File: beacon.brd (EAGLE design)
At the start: 40 x 25.3 mm, 49 parts, among them J1 5-5530843-0MALE, Q1 MMBT3904, Q2 DMG2302UK, U1 AOZ6662DI, U3 ATTINY85, U4 MS5637-02BA03, U5 SI4012, U6 MAAL-010704, U7 MIC5504

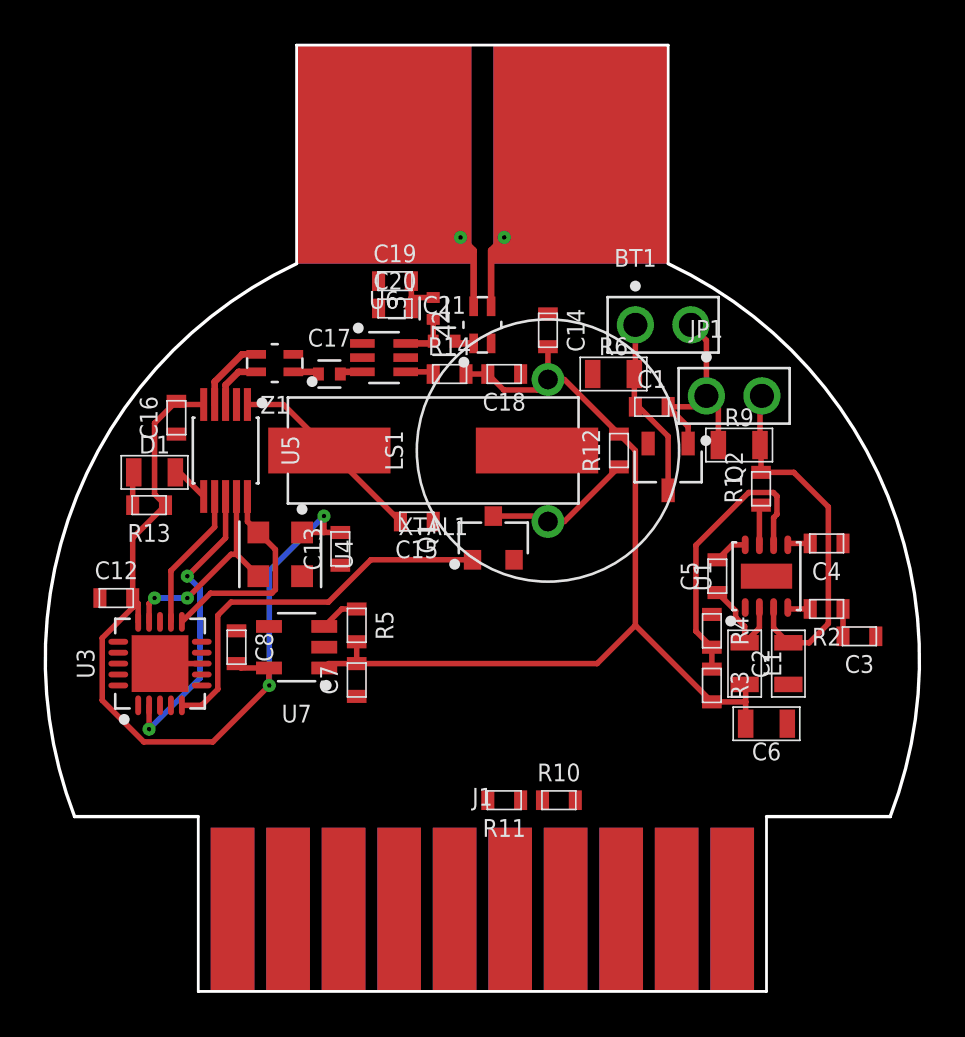
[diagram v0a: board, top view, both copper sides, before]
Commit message: Routed beacon
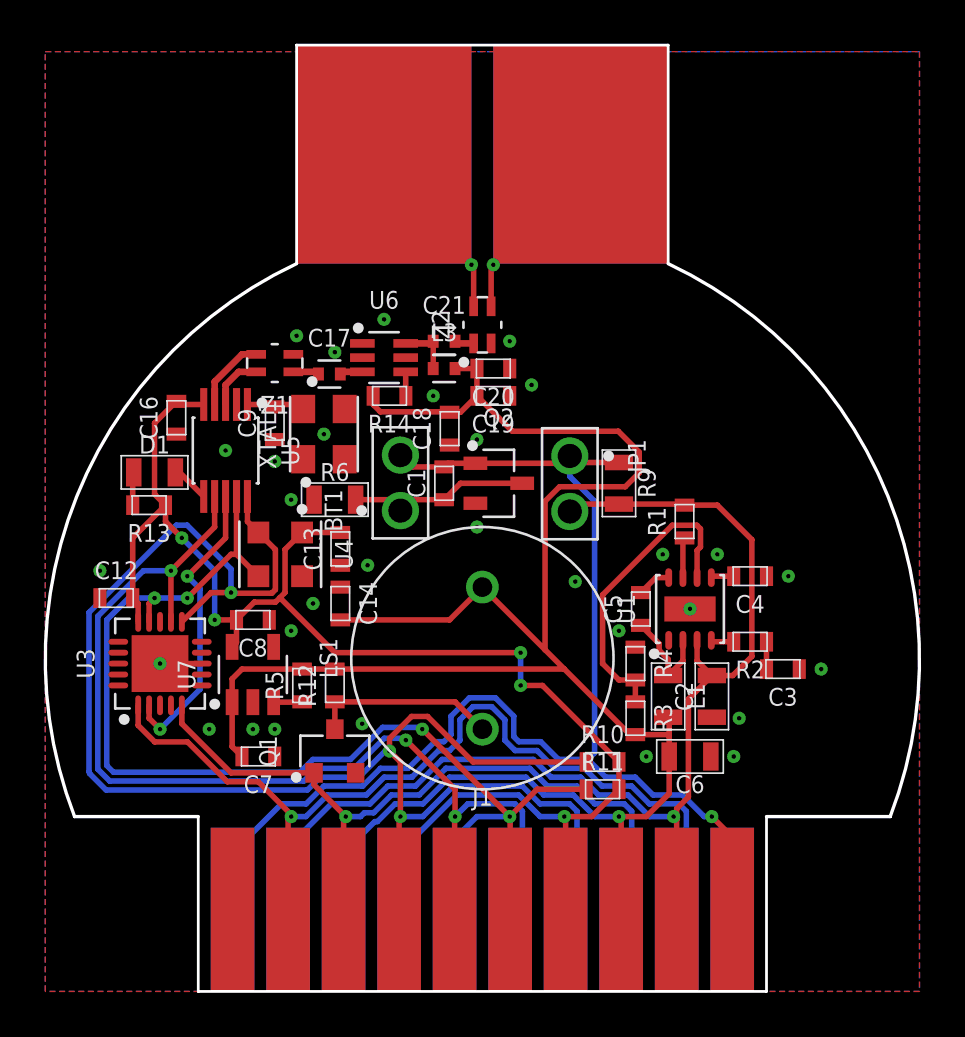
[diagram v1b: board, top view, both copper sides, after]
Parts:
- removed C15: 15pF, radio-tracker:0603
- added C9: 10pF, radio-tracker:0603
- XTAL1: device radio-tracker:ABLS -> radio-tracker:RH100
- moved R12 16.9 mm to (13.2, 14.0)
- moved C14 15.7 mm to (13.5, 17.8)
- moved R6 14.0 mm to (13.2, 22.5)
- moved BT1 13.7 mm to (16.2, 22.0), turned to 90 degrees
- moved Q1 12.2 mm to (13.2, 11.0)
- moved C1 10.1 mm to (18.2, 23.2), turned to 90 degrees
- moved LS1 9.96 mm to (20.0, 15.2)
- moved Q2 7.79 mm to (20.8, 23.2), turned to 0 degrees
- moved C19 6.91 mm to (20.5, 27.2), turned to 180 degrees
- moved JP1 6.83 mm to (24.0, 24.5), turned to 270 degrees
- moved R9 5.77 mm to (26.2, 23.2), turned to 270 degrees
- moved C7 5.70 mm to (9.75, 10.8), turned to 180 degrees
- moved C20 5.27 mm to (20.5, 28.5), turned to 180 degrees
- moved XTAL1 5.06 mm to (12.8, 25.5), turned to 90 degrees
- moved R11 4.53 mm to (25.5, 9.25), turned to 0 degrees
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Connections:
- net !RESET: now also J1.19, J1.9; no longer J1.16, J1.6
- net +3V3: now also J1.14, J1.4; no longer J1.1, J1.11
- net +5V: now also J1.13, J1.3; no longer J1.12, J1.2
- net +9V: now also J1.12, J1.2; no longer J1.13, J1.3
- net GND: now also C9.P$1, XTAL1.2, XTAL1.3; no longer C15.P$1
- net MISO/!PCINT1: now also J1.16, J1.6; no longer J1.18, J1.8
- net MOSI/SDA: now also J1.17, J1.7; no longer J1.19, J1.9
- net N$17: now also C9.P$2, XTAL1.4; no longer C15.P$2, XTAL1.2
- net OC1B: now also J1.18, J1.8; no longer J1.15, J1.5
- net SCLK/SCK: now also J1.15, J1.5; no longer J1.17, J1.7
- net VBAT: now also J1.1, J1.11; no longer J1.14, J1.4
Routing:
- net MOSI/SDA: track 9.68 -> 74.1 mm, vias 0 -> 3
- net VBAT: track 10.0 -> 62.0 mm, vias 0 -> 1
- net +5V: track 45.7 -> 94.4 mm, vias 0 -> 1
- net SCLK/SCK: track 9.83 -> 54.7 mm, vias 2 -> 4
- net MISO/!PCINT1: track 6.56 -> 49.8 mm, vias 0 -> 3
- net !RESET: track 0.00 -> 41.9 mm, vias 0 -> 1
- net +9V: track 16.7 -> 53.4 mm, vias 0 -> 1
- net +3V3: track 41.2 -> 70.0 mm, vias 2 -> 5
- net OC1B: track 18.0 -> 34.2 mm, vias 0 -> 1
- net N$30: track 8.65 -> 15.4 mm
- net N$17: track 9.22 -> 2.74 mm
- net N$31: track 8.95 -> 15.4 mm
- net N$15: track 6.89 -> 8.52 mm
- net N$7: track 13.0 -> 14.1 mm
- net N$9: track 1.82 -> 1.31 mm
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- added copper zone on layer 1, net GND
- added copper zone on layer 16, net GND
